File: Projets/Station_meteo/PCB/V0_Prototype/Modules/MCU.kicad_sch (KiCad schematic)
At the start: 36 parts, among them J1 SolderJumper_2_Bridged, J10 SolderJumper_2_Bridged, J11 SolderJumper_2_Bridged, J12 SolderJumper_2_Bridged, J13 SolderJumper_2_Bridged, J14 SolderJumper_2_Bridged, J15 SolderJumper_2_Bridged, J16 SolderJumper_2_Bridged, J17 SolderJumper_2_Bridged, J18 SolderJumper_2_Bridged, J19 SolderJumper_2_Bridged, J2 SolderJumper_2_Bridged, J20 SolderJumper_2_Bridged, J21 SolderJumper_2_Bridged, J22 SolderJumper_2_Bridged, J23 SolderJumper_2_Bridged, J3 SolderJumper_2_Bridged, J4 SolderJumper_2_Bridged, J5 SolderJumper_2_Bridged, J6 SolderJumper_2_Bridged, J7 SolderJumper_2_Bridged, J8 SolderJumper_2_Bridged, J9 SolderJumper_2_Bridged, T1 TP, T2 TP, T3 TP, T4 TP, T5 TP, T6 TP, T7 TP, T8 TP, U1 ATMEGA-328P

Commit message: Update PCB
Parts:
- removed T3, T6, T7, T8: TP, TestPoint:TestPoint_Pad_D1.0mm, symbol Connector:TestPoint
- added J31, J36, J37, J38: Conn_01x01_Pin, Connector_PinHeader_2.54mm:PinHeader_1x01_P2.54mm_Vertical, symbol Connector:Conn_01x01_Pin
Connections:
- net PB2-D10~: now also J38.1 (Pin_1)
- net PB3-D11-(SPI_MISO)~: now also J31.1 (Pin_1)
- net PB4-D12-(SPI_MOSI): now also J36.1 (Pin_1)
- net PB5-D13-(SPI_SCK): now also J37.1 (Pin_1)

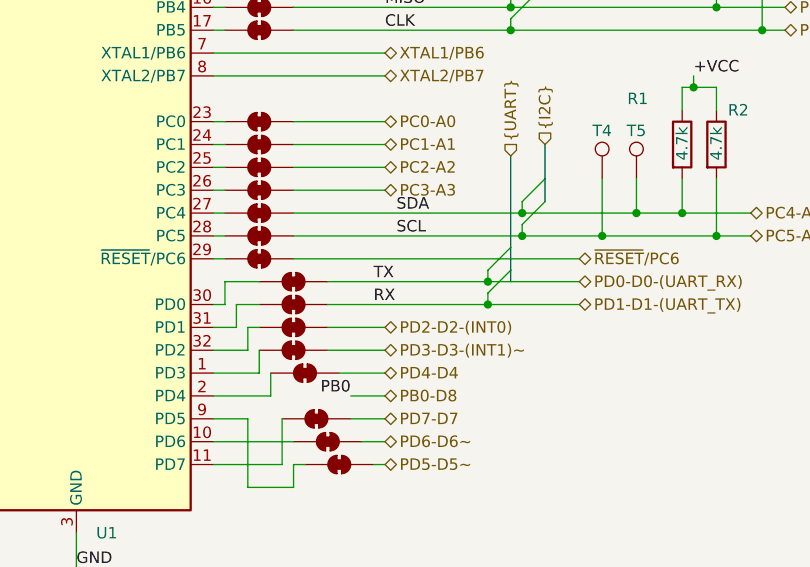
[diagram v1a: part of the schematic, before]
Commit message: Add V1 THT version
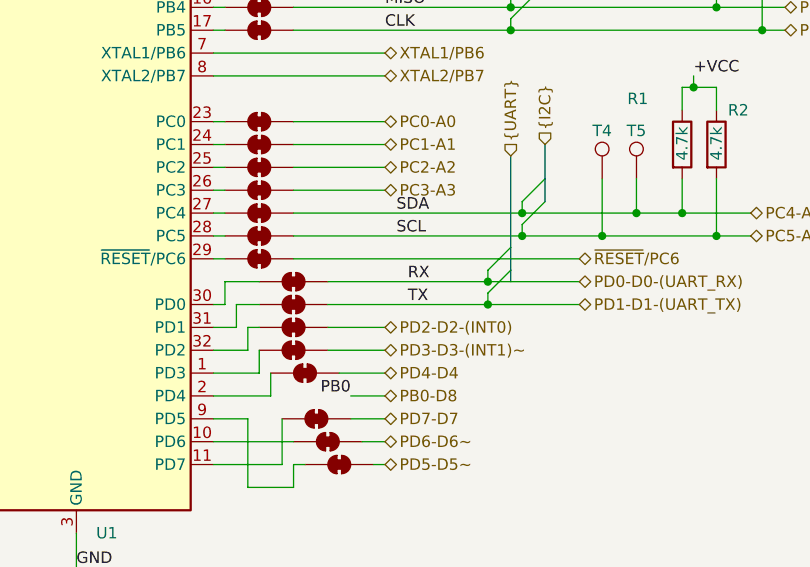
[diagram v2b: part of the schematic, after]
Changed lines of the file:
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@@
 	)
 	(label "RX"
-		(at 106.68 80.01 0)
+		(at 110.49 77.47 0)
 		(fields_autoplaced yes)
 		(effects
@@
 	)
 	(label "TX"
-		(at 106.68 77.47 0)
+		(at 110.49 80.01 0)
 		(fields_autoplaced yes)
 		(effects
